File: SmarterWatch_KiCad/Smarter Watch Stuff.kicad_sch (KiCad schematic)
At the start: 0 parts

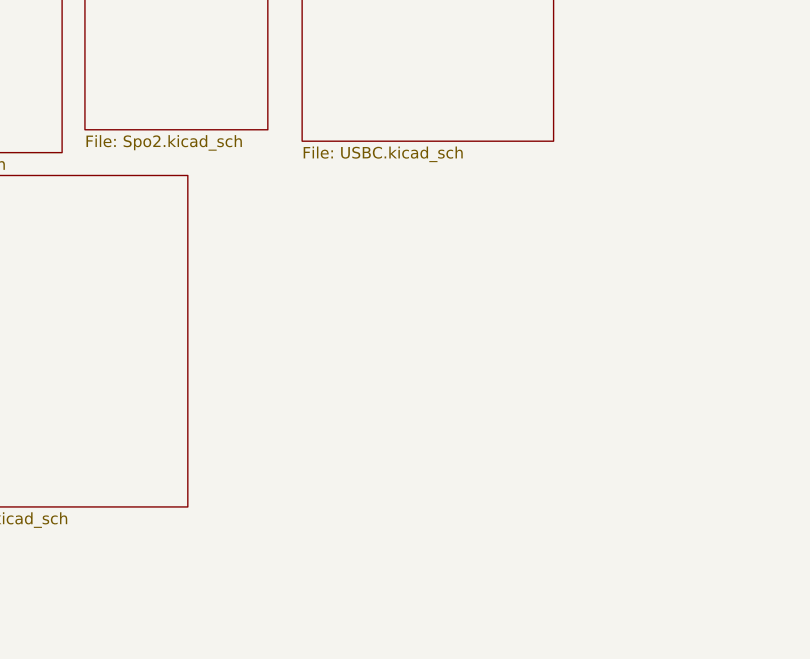
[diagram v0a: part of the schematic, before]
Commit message: Added Skin Temp
Added Skin Temp to schematic
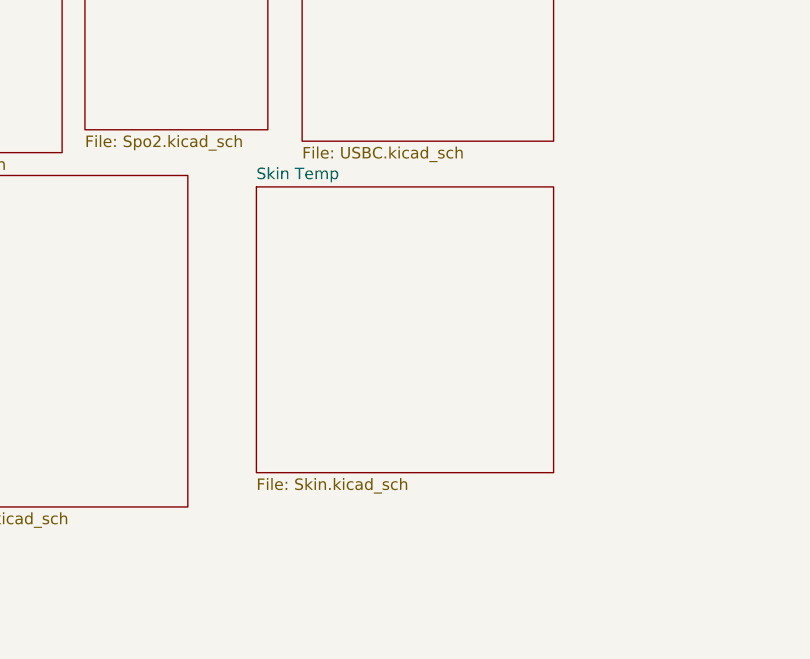
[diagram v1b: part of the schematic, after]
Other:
- added sheet Skin Temp (Skin.kicad_sch)
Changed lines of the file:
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@@
+	)
+	(sheet
+		(at 90.17 91.44)
+		(size 33.02 31.75)
+		(exclude_from_sim no)
+		(in_bom yes)
+		(on_board yes)
+		(dnp no)
+		(fields_autoplaced yes)
+		(stroke
+			(width 0.1524)
+			(type solid)
+		)
+		(fill
+			(color 0 0 0 0.0000)
+		)
+		(property "Sheetname" "Skin Temp"
+			(at 90.17 90.7284 0)
+			(effects
+				(font
+					(size 1.27 1.27)
+				)
+				(justify left bottom)
+			)
+		)
+		(property "Sheetfile" "Skin.kicad_sch"
+			(at 90.17 123.7746 0)
+			(effects
+				(font
+					(size 1.27 1.27)
+				)
+				(justify left top)
+			)
+		)
+		(instances
+			(project "Smarter Watch Stuff"
+				(path "/52181fb0-1be8-41da-83b2-7d5a62778ff4"
+					(page "18")
+				)
+			)
+		)
 	)
 	(sheet

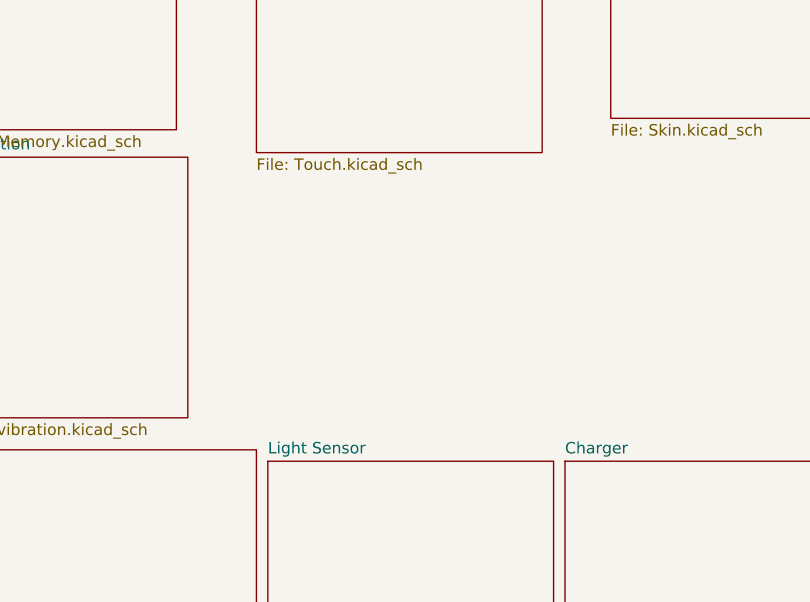
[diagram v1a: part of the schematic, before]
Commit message: BARO symbol
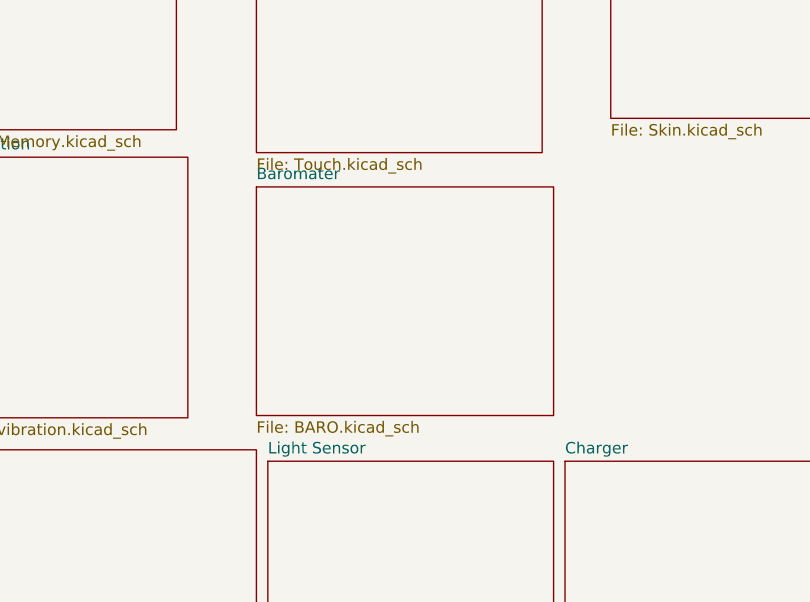
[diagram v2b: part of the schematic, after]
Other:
- added sheet Baromater (BARO.kicad_sch)
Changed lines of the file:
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@@
+	)
+	(sheet
+		(at 50.8 130.81)
+		(size 33.02 25.4)
+		(exclude_from_sim no)
+		(in_bom yes)
+		(on_board yes)
+		(dnp no)
+		(fields_autoplaced yes)
+		(stroke
+			(width 0.1524)
+			(type solid)
+		)
+		(fill
+			(color 0 0 0 0.0000)
+		)
+		(property "Sheetname" "Baromater"
+			(at 50.8 130.0984 0)
+			(effects
+				(font
+					(size 1.27 1.27)
+				)
+				(justify left bottom)
+			)
+		)
+		(property "Sheetfile" "BARO.kicad_sch"
+			(at 50.8 156.7946 0)
+			(effects
+				(font
+					(size 1.27 1.27)
+				)
+				(justify left top)
+			)
+		)
+		(instances
+			(project "Smarter Watch Stuff"
+				(path "/52181fb0-1be8-41da-83b2-7d5a62778ff4"
+					(page "19")
+				)
+			)
+		)
 	)
 	(sheet

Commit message: Magnetometor sheet
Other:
- added sheet Magnetometer (magnetometer.kicad_sch)
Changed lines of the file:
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@@
+	)
+	(sheet
+		(at 88.9 129.54)
+		(size 34.29 30.48)
+		(exclude_from_sim no)
+		(in_bom yes)
+		(on_board yes)
+		(dnp no)
+		(fields_autoplaced yes)
+		(stroke
+			(width 0.1524)
+			(type solid)
+		)
+		(fill
+			(color 0 0 0 0.0000)
+		)
+		(property "Sheetname" "Magnetometer"
+			(at 88.9 128.8284 0)
+			(effects
+				(font
+					(size 1.27 1.27)
+				)
+				(justify left bottom)
+			)
+		)
+		(property "Sheetfile" "magnetometer.kicad_sch"
+			(at 88.9 160.6046 0)
+			(effects
+				(font
+					(size 1.27 1.27)
+				)
+				(justify left top)
+			)
+		)
+		(instances
+			(project "Smarter Watch Stuff"
+				(path "/52181fb0-1be8-41da-83b2-7d5a62778ff4"
+					(page "20")
+				)
+			)
+		)
 	)
 	(sheet

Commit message: Lightning Sheet
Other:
- added sheet Lightning (Lightning.kicad_sch)
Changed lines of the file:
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@@
+	)
+	(sheet
+		(at 132.08 16.51)
+		(size 38.1 30.48)
+		(exclude_from_sim no)
+		(in_bom yes)
+		(on_board yes)
+		(dnp no)
+		(fields_autoplaced yes)
+		(stroke
+			(width 0.1524)
+			(type solid)
+		)
+		(fill
+			(color 0 0 0 0.0000)
+		)
+		(property "Sheetname" "Lightning"
+			(at 132.08 15.7984 0)
+			(effects
+				(font
+					(size 1.27 1.27)
+				)
+				(justify left bottom)
+			)
+		)
+		(property "Sheetfile" "Lightning.kicad_sch"
+			(at 132.08 47.5746 0)
+			(effects
+				(font
+					(size 1.27 1.27)
+				)
+				(justify left top)
+			)
+		)
+		(instances
+			(project "Smarter Watch Stuff"
+				(path "/52181fb0-1be8-41da-83b2-7d5a62778ff4"
+					(page "21")
+				)
+			)
+		)
 	)
 	(sheet

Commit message: Done part of CO2
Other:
- added sheet CO2 (CO2.kicad_sch)
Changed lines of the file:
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@@
+	)
+	(sheet
+		(at 134.62 53.34)
+		(size 40.64 38.1)
+		(exclude_from_sim no)
+		(in_bom yes)
+		(on_board yes)
+		(dnp no)
+		(fields_autoplaced yes)
+		(stroke
+			(width 0.1524)
+			(type solid)
+		)
+		(fill
+			(color 0 0 0 0.0000)
+		)
+		(property "Sheetname" "CO2"
+			(at 134.62 52.6284 0)
+			(effects
+				(font
+					(size 1.27 1.27)
+				)
+				(justify left bottom)
+			)
+		)
+		(property "Sheetfile" "CO2.kicad_sch"
+			(at 134.62 92.0246 0)
+			(effects
+				(font
+					(size 1.27 1.27)
+				)
+				(justify left top)
+			)
+		)
+		(instances
+			(project "Smarter Watch Stuff"
+				(path "/52181fb0-1be8-41da-83b2-7d5a62778ff4"
+					(page "22")
+				)
+			)
+		)
 	)
 	(sheet

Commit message: Clean Up
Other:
- added sheet Level Shifter (Level_Shifter.kicad_sch)
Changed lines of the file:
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@@
+	)
+	(sheet
+		(at 137.16 97.79)
+		(size 35.56 27.94)
+		(exclude_from_sim no)
+		(in_bom yes)
+		(on_board yes)
+		(dnp no)
+		(fields_autoplaced yes)
+		(stroke
+			(width 0.1524)
+			(type solid)
+		)
+		(fill
+			(color 0 0 0 0.0000)
+		)
+		(property "Sheetname" "Level Shifter"
+			(at 137.16 97.0784 0)
+			(effects
+				(font
+					(size 1.27 1.27)
+				)
+				(justify left bottom)
+			)
+		)
+		(property "Sheetfile" "Level_Shifter.kicad_sch"
+			(at 137.16 126.3146 0)
+			(effects
+				(font
+					(size 1.27 1.27)
+				)
+				(justify left top)
+			)
+		)
+		(instances
+			(project "Smarter Watch Stuff"
+				(path "/52181fb0-1be8-41da-83b2-7d5a62778ff4"
+					(page "23")
+				)
+			)
+		)
 	)
 	(sheet

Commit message: order
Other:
- sheet Baromater renamed Barometer
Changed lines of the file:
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@@
 			(color 0 0 0 0.0000)
 		)
-		(property "Sheetname" "Baromater"
+		(property "Sheetname" "Barometer"
 			(at 50.8 130.0984 0)
 			(effects

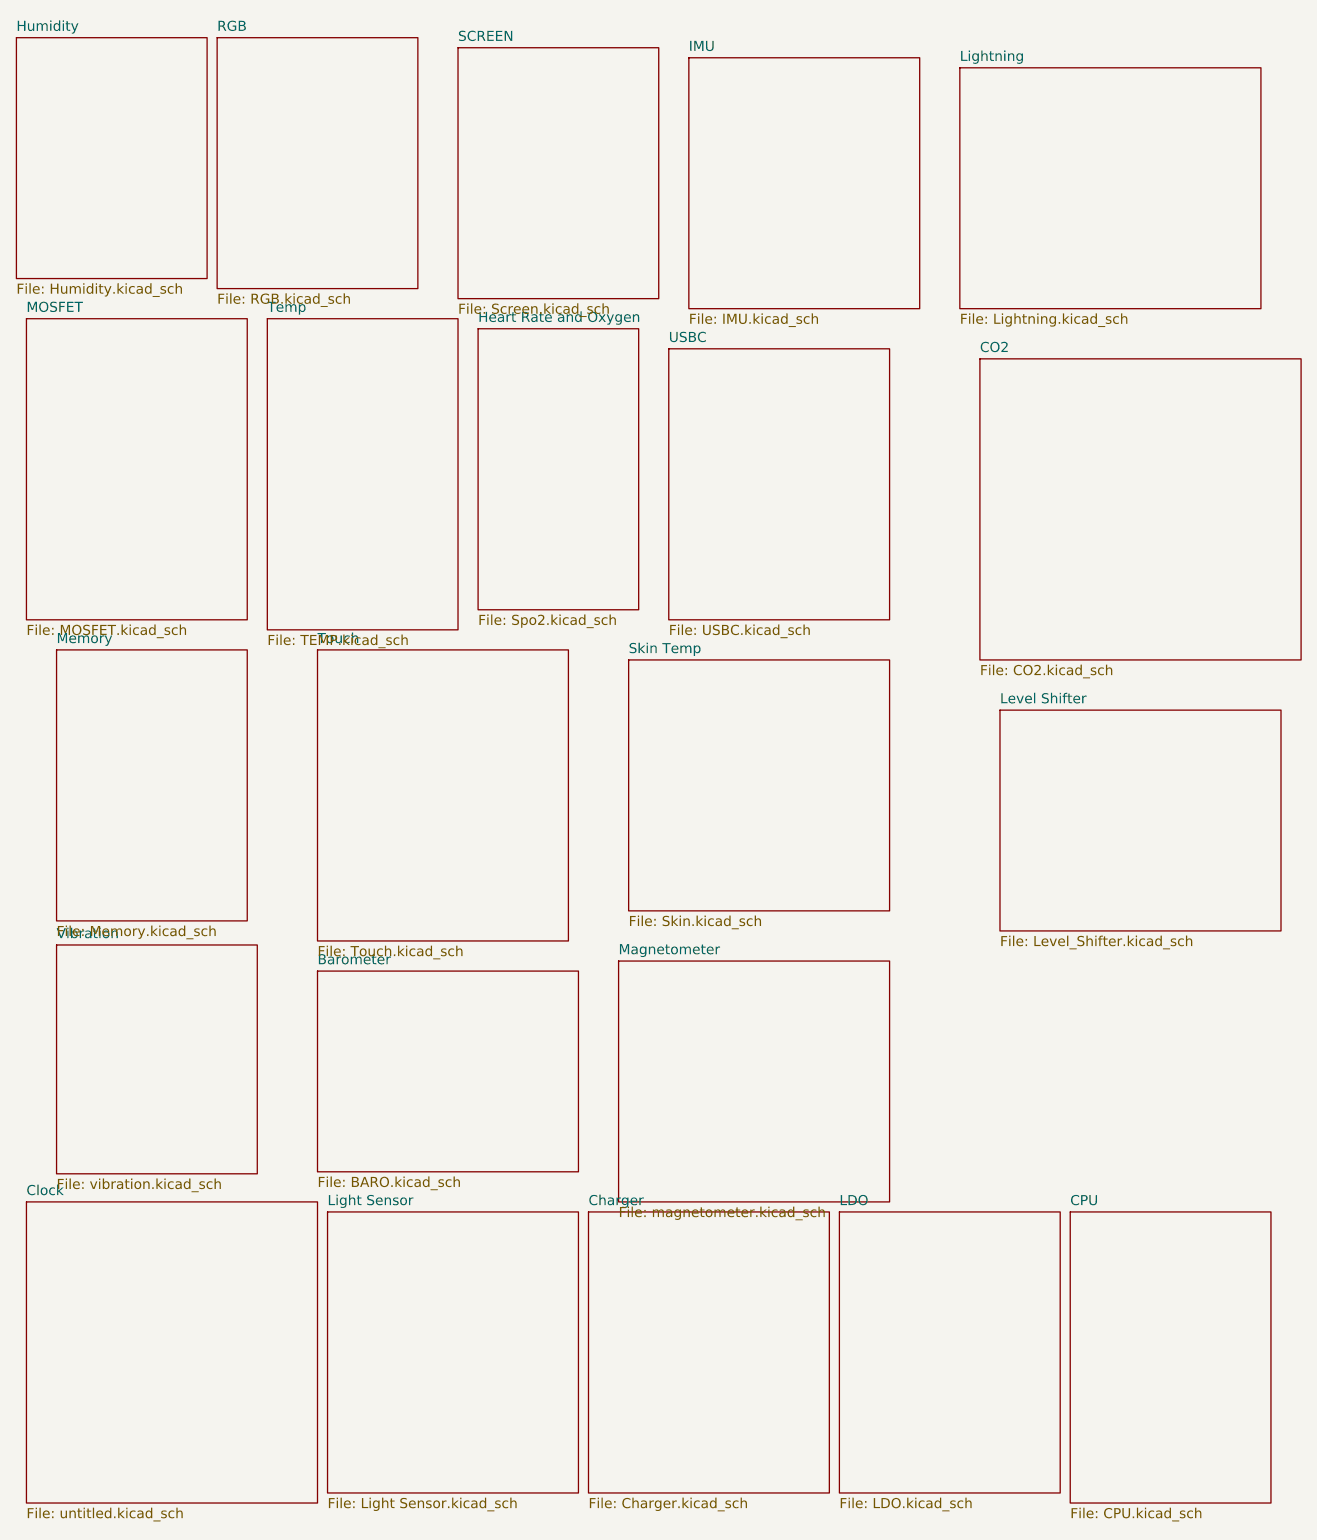
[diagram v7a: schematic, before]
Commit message: Label Jumpers
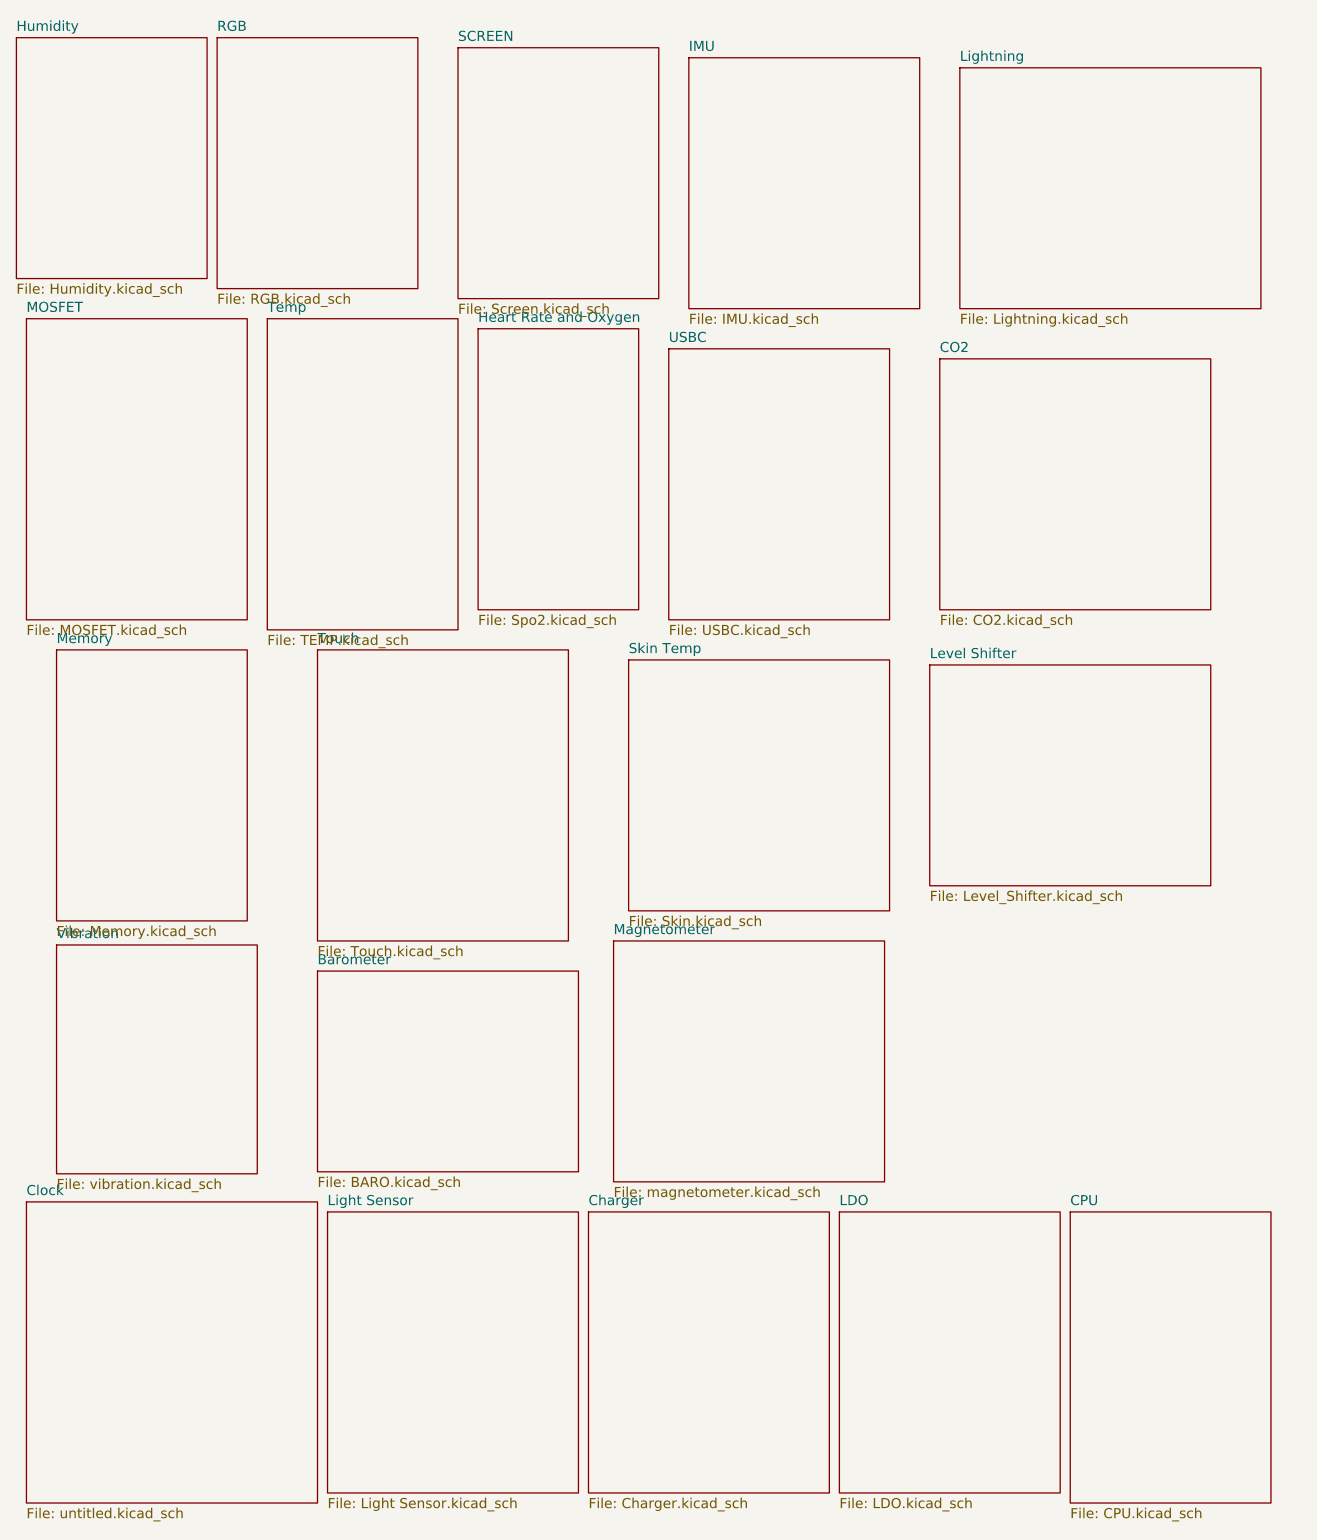
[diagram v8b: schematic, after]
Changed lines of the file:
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@@
 	)
 	(sheet
-		(at 134.62 53.34)
-		(size 40.64 38.1)
+		(at 129.54 53.34)
+		(size 34.29 31.75)
 		(exclude_from_sim no)
 		(in_bom yes)
@@
 		)
 		(property "Sheetname" "CO2"
-			(at 134.62 52.6284 0)
+			(at 129.54 52.6284 0)
 			(effects
 				(font
@@
 		)
 		(property "Sheetfile" "CO2.kicad_sch"
-			(at 134.62 92.0246 0)
+			(at 129.54 85.6746 0)
 			(effects
 				(font
@@
 	)
 	(sheet
-		(at 137.16 97.79)
+		(at 128.27 92.075)
 		(size 35.56 27.94)
 		(exclude_from_sim no)
@@
 		)
 		(property "Sheetname" "Level Shifter"
-			(at 137.16 97.0784 0)
+			(at 128.27 91.3634 0)
 			(effects
 				(font
@@
 		)
 		(property "Sheetfile" "Level_Shifter.kicad_sch"
-			(at 137.16 126.3146 0)
+			(at 128.27 120.5996 0)
 			(effects
 				(font
@@
 	)
 	(sheet
-		(at 88.9 129.54)
+		(at 88.265 127)
 		(size 34.29 30.48)
 		(exclude_from_sim no)
@@
 		)
 		(property "Sheetname" "Magnetometer"
-			(at 88.9 128.8284 0)
+			(at 88.265 126.2884 0)
 			(effects
 				(font
@@
 		)
 		(property "Sheetfile" "magnetometer.kicad_sch"
-			(at 88.9 160.6046 0)
-			(effects
-				(font
+			(at 88.265 158.0646 0)
+			(effects
+				(font
